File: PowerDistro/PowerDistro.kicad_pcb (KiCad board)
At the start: 2 copper layers, 100 x 85 mm, 18 parts, among them J3 12V, Q1 DMT6009LCT, U4 Optoisolators

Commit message: Updated powerdistro
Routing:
- net -BATT: vias 3 -> 7
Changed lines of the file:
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@@
+	)
+	(via
+		(at 185.928 56.896)
+		(size 0.6)
+		(drill 0.3)
+		(layers "F.Cu" "B.Cu")
+		(free yes)
+		(net 2)
 	)
 	(via
@@
 	)
 	(via
+		(at 132.5 55)
+		(size 0.6)
+		(drill 0.3)
+		(layers "F.Cu" "B.Cu")
+		(net 2)
+	)
+	(via
 		(at 200 56)
 		(size 0.6)
 		(drill 0.3)
+		(layers "F.Cu" "B.Cu")
+		(free yes)
+		(net 2)
+	)
+	(via
+		(at 213.868 58.166)
+		(size 0.6)
+		(drill 0.3)
+		(layers "F.Cu" "B.Cu")
+		(free yes)
+		(net 2)
+	)
+	(via
+		(at 190.246 48.768)
+		(size 0.6)
+		(drill 0.3)

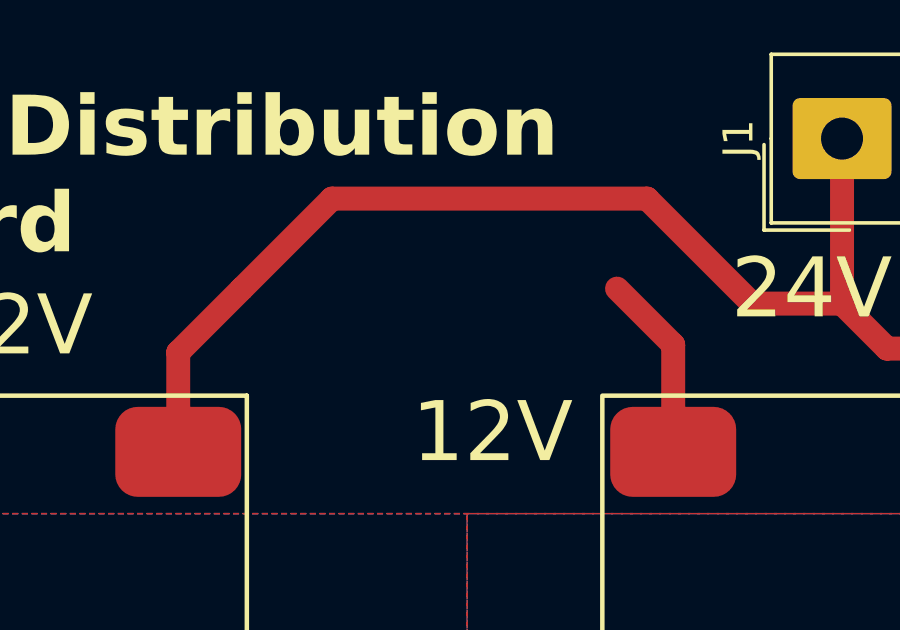
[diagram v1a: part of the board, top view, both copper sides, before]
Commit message: Fixed grounding problem in middle board
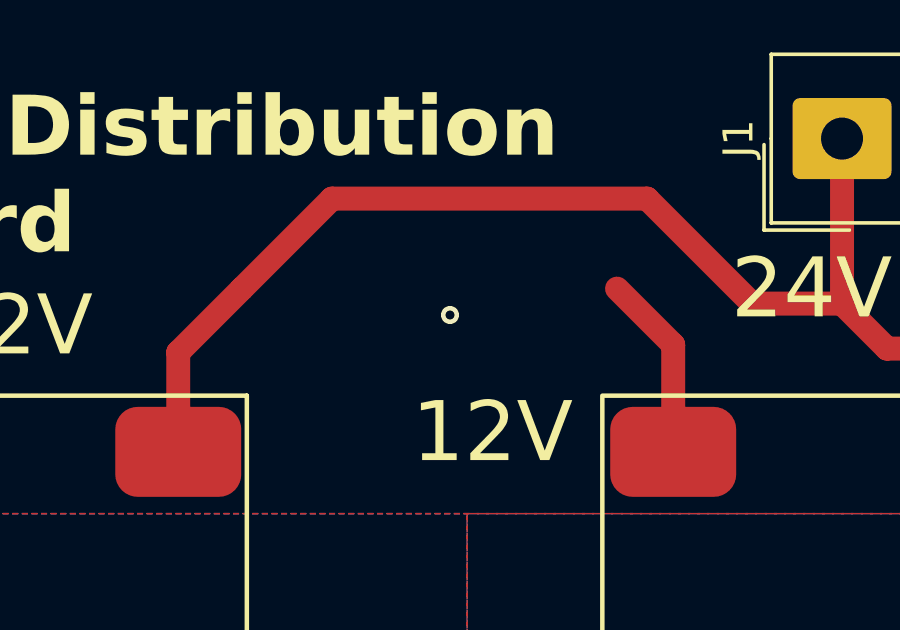
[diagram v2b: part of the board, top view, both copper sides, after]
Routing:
- net -BATT: vias 7 -> 8
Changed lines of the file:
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@@
+	)
+	(via
+		(at 154.432 55.88)
+		(size 0.6)
+		(drill 0.3)
+		(layers "F.Cu" "B.Cu")
+		(free yes)
+		(net 2)
 	)
 	(via

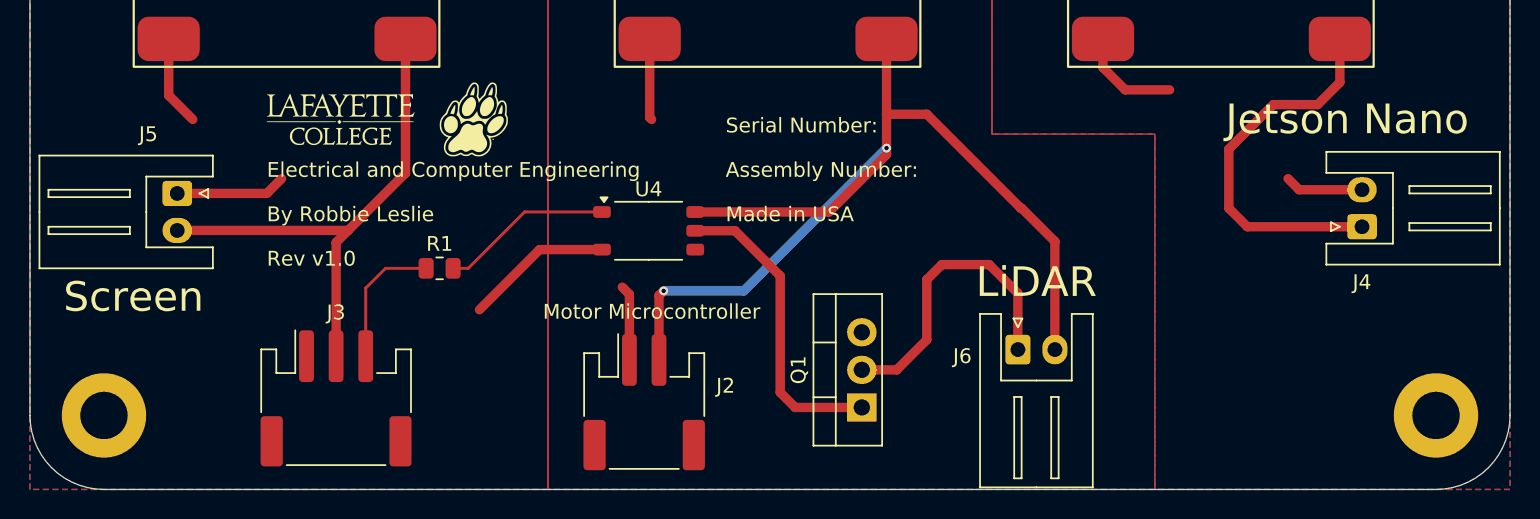
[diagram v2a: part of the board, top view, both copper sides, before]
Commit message: Swapped to XH-A-1 connector and added mounting hole stencil cutouts
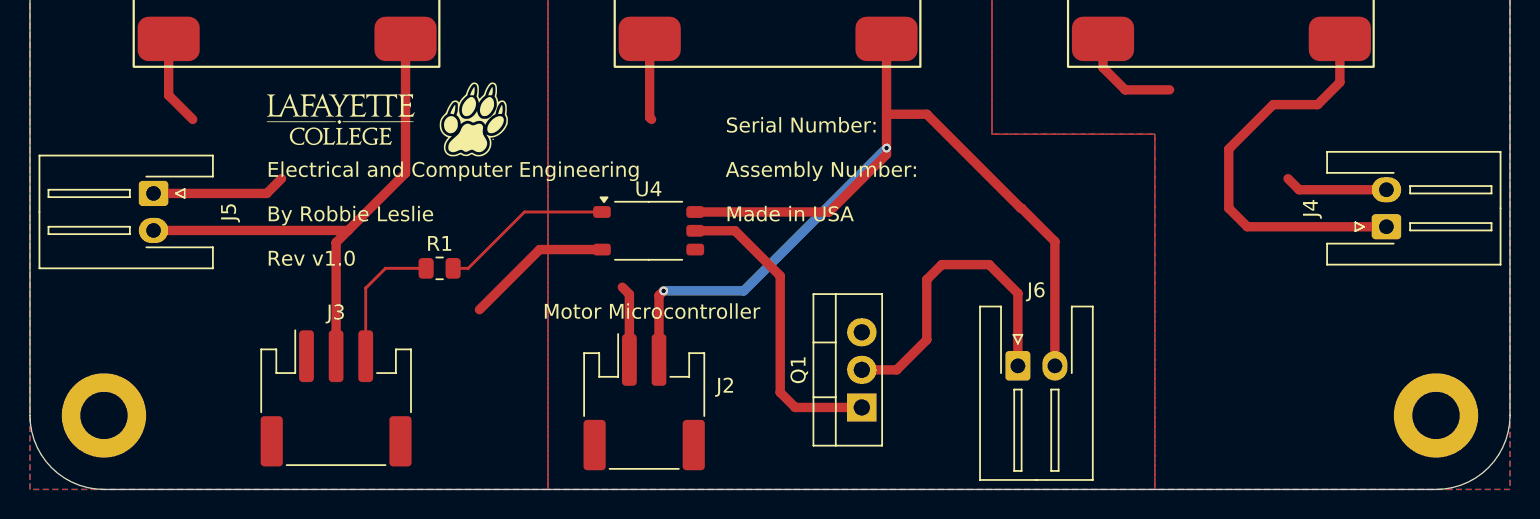
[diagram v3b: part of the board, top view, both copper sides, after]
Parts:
- J4, J5, J6: footprint Connector_JST:JST_XH_S2B-XH-A_1x02_P2.50mm_Horizontal -> Connector_JST:JST_XH_S2B-XH-A-1_1x02_P2.50mm_Horizontal
- moved J4 1.65 mm to (211.7, 112.2)
- moved J5 1.60 mm to (128.3, 110.0)
- moved J6 1.10 mm to (186.8, 121.7)
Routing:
- net /19V GND: track 12.4 -> 14.0 mm
- net /19V: track 25.8 -> 27.5 mm
- net /Reg1 GND: track 23.5 -> 25.1 mm
- net /12V Reg1: track 34.9 -> 36.5 mm
- net /12V Reg2: track 68.4 -> 69.5 mm
- net /LiDAR GND: track 20.5 -> 21.6 mm

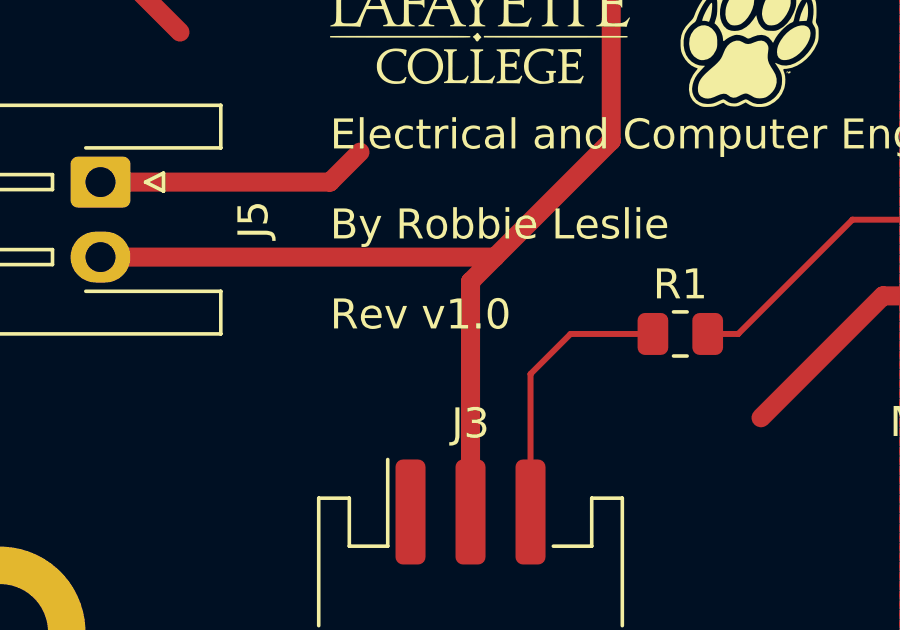
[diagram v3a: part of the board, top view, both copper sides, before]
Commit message: Updated rivision silkscreen
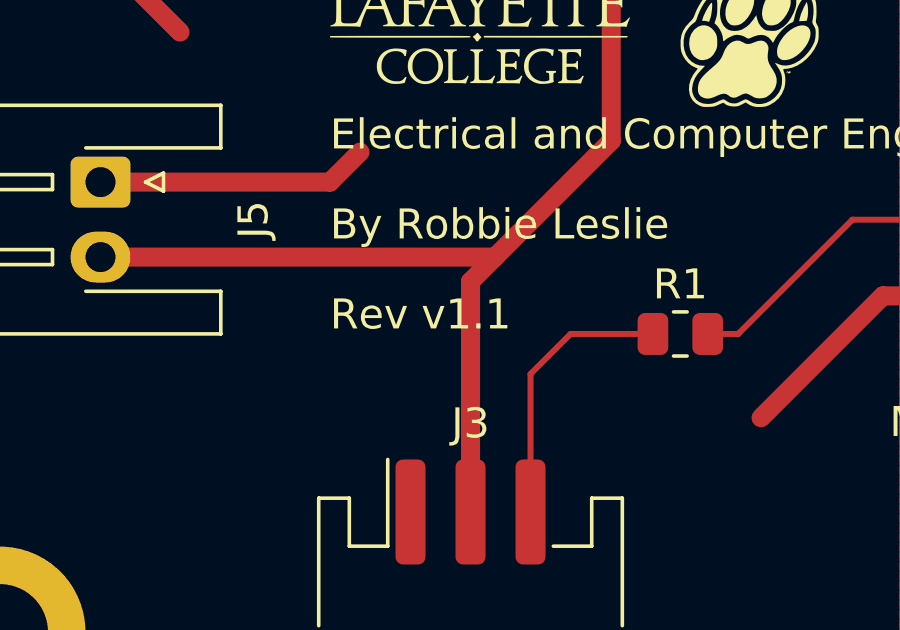
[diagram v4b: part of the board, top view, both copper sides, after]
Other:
- board text added: "Rev v1.1"
- board text removed: "Rev v1.0"
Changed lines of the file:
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@@
 	(title_block
 		(title "Power Distribution Board")
-		(date "2025-03-06")
+		(date "2025-03-07")
 		(rev "v1.1")
 		(company "Lafayette College")
@@
 			(size 2.7 3.3)
 			(drill 1.4)
-			(layers "*.Cu" "*.Mask")
+			(layers "*.Cu" "*.Mask" "In1.Cu" "In2.Cu" "In3.Cu" "In4.Cu" "In5.Cu" "In6.Cu"
+				"In7.Cu" "In8.Cu" "In9.Cu" "In10.Cu" "In11.Cu" "In12.Cu" "In13.Cu" "In14.Cu"
+				"In15.Cu" "In16.Cu" "In17.Cu" "In18.Cu" "In19.Cu" "In20.Cu" "In21.Cu"
+				"In22.Cu" "In23.Cu" "In24.Cu" "In25.Cu" "In26.Cu" "In27.Cu" "In28.Cu"
+				"In29.Cu" "In30.Cu"
+			)
 			(remove_unused_layers no)
 			(roundrect_rratio 0.092593)
@@
 			(size 2.7 3.3)
 			(drill 1.4)
-			(layers "*.Cu" "*.Mask")
+			(layers "*.Cu" "*.Mask" "In1.Cu" "In2.Cu" "In3.Cu" "In4.Cu" "In5.Cu" "In6.Cu"
+				"In7.Cu" "In8.Cu" "In9.Cu" "In10.Cu" "In11.Cu" "In12.Cu" "In13.Cu" "In14.Cu"
+				"In15.Cu" "In16.Cu" "In17.Cu" "In18.Cu" "In19.Cu" "In20.Cu" "In21.Cu"
+				"In22.Cu" "In23.Cu" "In24.Cu" "In25.Cu" "In26.Cu" "In27.Cu" "In28.Cu"
+				"In29.Cu" "In30.Cu"
+			)
 			(remove_unused_layers no)
 			(net 2 "-BATT")
@@
 			(size 1.7 2)
 			(drill 1)
-			(layers "*.Cu" "*.Mask")
+			(layers "*.Cu" "*.Mask" "In1.Cu" "In2.Cu" "In3.Cu" "In4.Cu" "In5.Cu" "In6.Cu"
+				"In7.Cu" "In8.Cu" "In9.Cu" "In10.Cu" "In11.Cu" "In12.Cu" "In13.Cu" "In14.Cu"
+				"In15.Cu" "In16.Cu" "In17.Cu" "In18.Cu" "In19.Cu" "In20.Cu" "In21.Cu"
+				"In22.Cu" "In23.Cu" "In24.Cu" "In25.Cu" "In26.Cu" "In27.Cu" "In28.Cu"
+				"In29.Cu" "In30.Cu"
+			)
 			(remove_unused_layers no)
 			(roundrect_rratio 0.147059)
@@
 			(size 1.7 2)
 			(drill 1)
-			(layers "*.Cu" "*.Mask")
+			(layers "*.Cu" "*.Mask" "In1.Cu" "In2.Cu" "In3.Cu" "In4.Cu" "In5.Cu" "In6.Cu"
+				"In7.Cu" "In8.Cu" "In9.Cu" "In10.Cu" "In11.Cu" "In12.Cu" "In13.Cu" "In14.Cu"
+				"In15.Cu" "In16.Cu" "In17.Cu" "In18.Cu" "In19.Cu" "In20.Cu" "In21.Cu"
+				"In22.Cu" "In23.Cu" "In24.Cu" "In25.Cu" "In26.Cu" "In27.Cu" "In28.Cu"
+				"In29.Cu" "In30.Cu"
+			)
 			(remove_unused_layers no)
 			(net 4 "/12V Reg2")
@@
 			(size 5.7 5.7)
 			(drill 3.2)
-			(layers "*.Cu" "*.Mask")
+			(layers "*.Cu" "*.Mask" "In1.Cu" "In2.Cu" "In3.Cu" "In4.Cu" "In5.Cu" "In6.Cu"
+				"In7.Cu" "In8.Cu" "In9.Cu" "In10.Cu" "In11.Cu" "In12.Cu" "In13.Cu" "In14.Cu"
+				"In15.Cu" "In16.Cu" "In17.Cu" "In18.Cu" "In19.Cu" "In20.Cu" "In21.Cu"
+				"In22.Cu" "In23.Cu" "In24.Cu" "In25.Cu" "In26.Cu" "In27.Cu" "In28.Cu"
+				"In29.Cu" "In30.Cu"
+			)
 			(remove_unused_layers no)
 		)
@@
 			(size 1.905 2)
 			(drill 1.1)
-			(layers "*.Cu" "*.Mask")
+			(layers "*.Cu" "*.Mask" "In1.Cu" "In2.Cu" "In3.Cu" "In4.Cu" "In5.Cu" "In6.Cu"
+				"In7.Cu" "In8.Cu" "In9.Cu" "In10.Cu" "In11.Cu" "In12.Cu" "In13.Cu" "In14.Cu"
+				"In15.Cu" "In16.Cu" "In17.Cu" "In18.Cu" "In19.Cu" "In20.Cu" "In21.Cu"
+				"In22.Cu" "In23.Cu" "In24.Cu" "In25.Cu" "In26.Cu" "In27.Cu" "In28.Cu"
+				"In29.Cu" "In30.Cu"
+			)
 			(remove_unused_layers no)
 			(net 11 "/LiDAR Wire")
@@
 			(size 1.905 2)
 			(drill 1.1)
-			(layers "*.Cu" "*.Mask")
+			(layers "*.Cu" "*.Mask" "In1.Cu" "In2.Cu" "In3.Cu" "In4.Cu" "In5.Cu" "In6.Cu"
+				"In7.Cu" "In8.Cu" "In9.Cu" "In10.Cu" "In11.Cu" "In12.Cu" "In13.Cu" "In14.Cu"
+				"In15.Cu" "In16.Cu" "In17.Cu" "In18.Cu" "In19.Cu" "In20.Cu" "In21.Cu"
+				"In22.Cu" "In23.Cu" "In24.Cu" "In25.Cu" "In26.Cu" "In27.Cu" "In28.Cu"
+				"In29.Cu" "In30.Cu"
+			)
 			(remove_unused_layers no)
 			(net 10 "/LiDAR GND")
@@
 			(size 1.905 2)
 			(drill 1.1)
-			(layers "*.Cu" "*.Mask")
+			(layers "*.Cu" "*.Mask" "In1.Cu" "In2.Cu" "In3.Cu" "In4.Cu" "In5.Cu" "In6.Cu"
+				"In7.Cu" "In8.Cu" "In9.Cu" "In10.Cu" "In11.Cu" "In12.Cu" "In13.Cu" "In14.Cu"
+				"In15.Cu" "In16.Cu" "In17.Cu" "In18.Cu" "In19.Cu" "In20.Cu" "In21.Cu"
+				"In22.Cu" "In23.Cu" "In24.Cu" "In25.Cu" "In26.Cu" "In27.Cu" "In28.Cu"
+				"In29.Cu" "In30.Cu"
+			)
 			(remove_unused_layers no)
 			(net 3 "/Reg2 GND")
@@
 			(size 5.7 5.7)
 			(drill 3.2)
-			(layers "*.Cu" "*.Mask")
+			(layers "*.Cu" "*.Mask" "In1.Cu" "In2.Cu" "In3.Cu" "In4.Cu" "In5.Cu" "In6.Cu"
+				"In7.Cu" "In8.Cu" "In9.Cu" "In10.Cu" "In11.Cu" "In12.Cu" "In13.Cu" "In14.Cu"
+				"In15.Cu" "In16.Cu" "In17.Cu" "In18.Cu" "In19.Cu" "In20.Cu" "In21.Cu"
+				"In22.Cu" "In23.Cu" "In24.Cu" "In25.Cu" "In26.Cu" "In27.Cu" "In28.Cu"
+				"In29.Cu" "In30.Cu"
+			)
 			(remove_unused_layers no)
 		)
@@
 			(size 5.7 5.7)
 			(drill 3.2)
-			(layers "*.Cu" "*.Mask")
+			(layers "*.Cu" "*.Mask" "In1.Cu" "In2.Cu" "In3.Cu" "In4.Cu" "In5.Cu" "In6.Cu"
+				"In7.Cu" "In8.Cu" "In9.Cu" "In10.Cu" "In11.Cu" "In12.Cu" "In13.Cu" "In14.Cu"
+				"In15.Cu" "In16.Cu" "In17.Cu" "In18.Cu" "In19.Cu" "In20.Cu" "In21.Cu"
+				"In22.Cu" "In23.Cu" "In24.Cu" "In25.Cu" "In26.Cu" "In27.Cu" "In28.Cu"
+				"In29.Cu" "In30.Cu"
+			)
 			(remove_unused_layers no)
 		)
@@
 			(size 5.7 5.7)
 			(drill 3.2)
-			(layers "*.Cu" "*.Mask")
+			(layers "*.Cu" "*.Mask" "In1.Cu" "In2.Cu" "In3.Cu" "In4.Cu" "In5.Cu" "In6.Cu"
+				"In7.Cu" "In8.Cu" "In9.Cu" "In10.Cu" "In11.Cu" "In12.Cu" "In13.Cu" "In14.Cu"
+				"In15.Cu" "In16.Cu" "In17.Cu" "In18.Cu" "In19.Cu" "In20.Cu" "In21.Cu"
+				"In22.Cu" "In23.Cu" "In24.Cu" "In25.Cu" "In26.Cu" "In27.Cu" "In28.Cu"
+				"In29.Cu" "In30.Cu"
+			)
 			(remove_unused_layers no)
 		)
@@
 			(size 1.7 2)
 			(drill 1)
-			(layers "*.Cu" "*.Mask")
+			(layers "*.Cu" "*.Mask" "In1.Cu" "In2.Cu" "In3.Cu" "In4.Cu" "In5.Cu" "In6.Cu"
+				"In7.Cu" "In8.Cu" "In9.Cu" "In10.Cu" "In11.Cu" "In12.Cu" "In13.Cu" "In14.Cu"
+				"In15.Cu" "In16.Cu" "In17.Cu" "In18.Cu" "In19.Cu" "In20.Cu" "In21.Cu"
+				"In22.Cu" "In23.Cu" "In24.Cu" "In25.Cu" "In26.Cu" "In27.Cu" "In28.Cu"
+				"In29.Cu" "In30.Cu"
+			)
 			(remove_unused_layers no)
 			(roundrect_rratio 0.147059)
@@
 			(size 1.7 2)
 			(drill 1)
-			(layers "*.Cu" "*.Mask")
+			(layers "*.Cu" "*.Mask" "In1.Cu" "In2.Cu" "In3.Cu" "In4.Cu" "In5.Cu" "In6.Cu"
+				"In7.Cu" "In8.Cu" "In9.Cu" "In10.Cu" "In11.Cu" "In12.Cu" "In13.Cu" "In14.Cu"
+				"In15.Cu" "In16.Cu" "In17.Cu" "In18.Cu" "In19.Cu" "In20.Cu" "In21.Cu"
+				"In22.Cu" "In23.Cu" "In24.Cu" "In25.Cu" "In26.Cu" "In27.Cu" "In28.Cu"
+				"In29.Cu" "In30.Cu"
+			)
 			(remove_unused_layers no)
 			(net 5 "/12V Reg1")
@@
 			(size 1.7 2)
 			(drill 1)
-			(layers "*.Cu" "*.Mask")
+			(layers "*.Cu" "*.Mask" "In1.Cu" "In2.Cu" "In3.Cu" "In4.Cu" "In5.Cu" "In6.Cu"
+				"In7.Cu" "In8.Cu" "In9.Cu" "In10.Cu" "In11.Cu" "In12.Cu" "In13.Cu" "In14.Cu"
+				"In15.Cu" "In16.Cu" "In17.Cu" "In18.Cu" "In19.Cu" "In20.Cu" "In21.Cu"
+				"In22.Cu" "In23.Cu" "In24.Cu" "In25.Cu" "In26.Cu" "In27.Cu" "In28.Cu"
+				"In29.Cu" "In30.Cu"
+			)
 			(remove_unused_layers no)
 			(roundrect_rratio 0.147059)
@@
 			(size 1.7 2)
 			(drill 1)
-			(layers "*.Cu" "*.Mask")
+			(layers "*.Cu" "*.Mask" "In1.Cu" "In2.Cu" "In3.Cu" "In4.Cu" "In5.Cu" "In6.Cu"
+				"In7.Cu" "In8.Cu" "In9.Cu" "In10.Cu" "In11.Cu" "In12.Cu" "In13.Cu" "In14.Cu"
+				"In15.Cu" "In16.Cu" "In17.Cu" "In18.Cu" "In19.Cu" "In20.Cu" "In21.Cu"
+				"In22.Cu" "In23.Cu" "In24.Cu" "In25.Cu" "In26.Cu" "In27.Cu" "In28.Cu"
+				"In29.Cu" "In30.Cu"
+			)
 			(remove_unused_layers no)
 			(net 7 "/19V GND")
@@
 		)
 	)
-	(gr_text "Rev v1.0"
+	(gr_text "Rev v1.1"
 		(at 218 96 0)
 		(layer "B.SilkS")
@@
 		)
 	)
-	(gr_text "Rev v1.0"
+	(gr_text "Rev v1.1"
 		(at 136 115 0)
 		(layer "F.SilkS")
@@
 		(net 7)
 		(net_name "/19V GND")
-		(layers "F&B.Cu")
+		(layers "F.Cu" "B.Cu")
 		(hatch edge 0.5)
 		(priority 3)
@@
 		(net 2)
 		(net_name "-BATT")
-		(layers "F&B.Cu")
+		(layers "F.Cu" "B.Cu")
 		(hatch edge 0.5)
 		(priority 4)
@@
 		(net 6)
 		(net_name "/Reg1 GND")
-		(layers "F&B.Cu")
+		(layers "F.Cu" "B.Cu")
 		(hatch edge 0.5)
 		(priority 1)
@@
 		(net 3)
 		(net_name "/Reg2 GND")
-		(layers "F&B.Cu")
+		(layers "F.Cu" "B.Cu")
 		(hatch edge 0.5)
 		(connect_pads
